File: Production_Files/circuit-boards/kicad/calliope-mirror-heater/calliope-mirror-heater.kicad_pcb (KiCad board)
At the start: 2 copper layers, 49 x 67 mm, 67 parts, among them J1 USB_C_Receptacle_USB2.0_16P, J2 Conn_02x15_Odd_Even, SW1 select-heater-power-source, U1 LM358DR2G, U2 TP5709S5, U3 XC6206P332MR-G, U4 GAQY212GSX

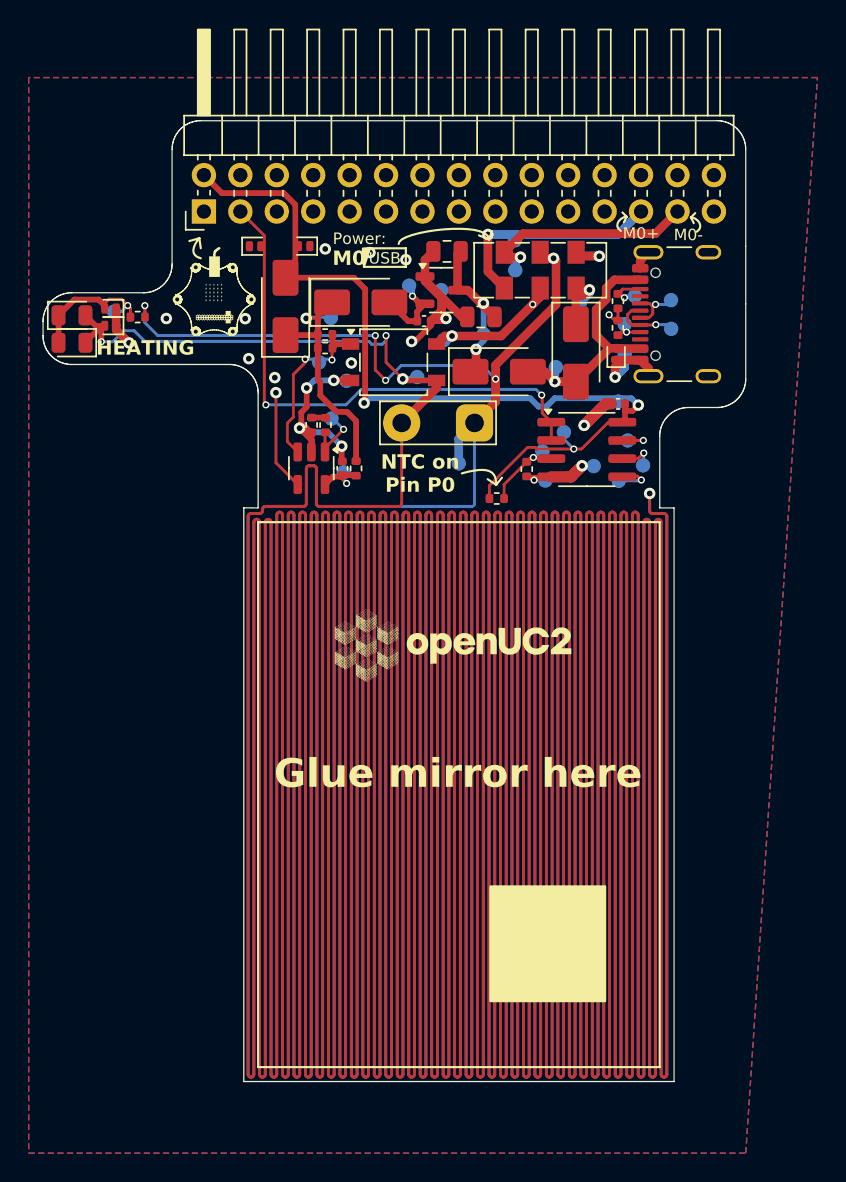
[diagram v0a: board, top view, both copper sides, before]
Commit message: Finished Rev B: correct slide-switch fp
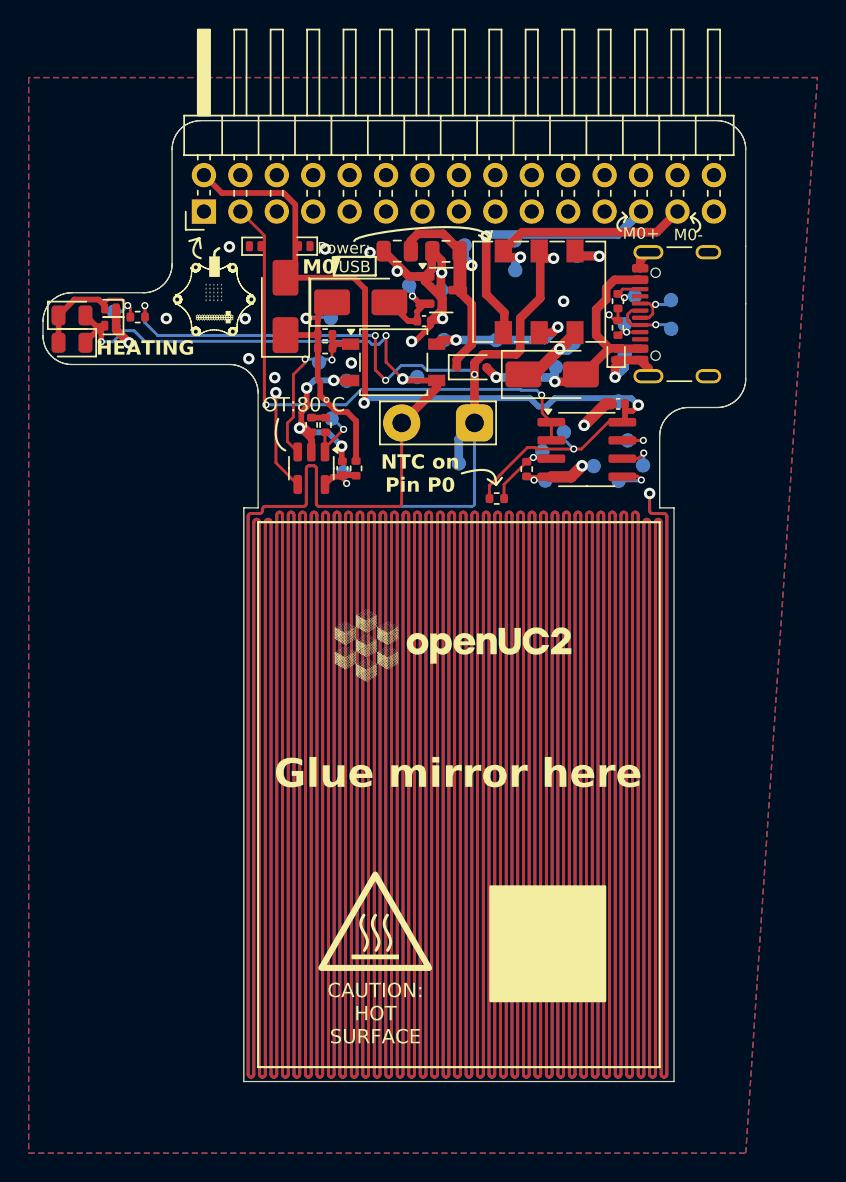
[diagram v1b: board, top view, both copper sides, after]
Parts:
- D4: value SS34 -> 1N5819WS; footprint Diode_SMD:D_SMA -> Diode_SMD:D_SOD-323
- moved C1 7.42 mm to (110.7, 82.1)
- moved TP10 6.35 mm to (115.4, 81.7)
- moved TP24 4.98 mm to (117.6, 88.3)
- moved TP25 2.83 mm to (123.0, 88.5)
- moved D7 2.24 mm to (121.5, 90.7), turned to 0 degrees
- moved D4 1.93 mm to (115.9, 90.2)
- moved SW1 1.50 mm to (120.6, 84.9)
- moved C3 0.07 mm to (114.1, 82.1)
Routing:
- net Net-(D4-K): track 11.4 -> 19.1 mm, vias 2 -> 1
- net GND: track 58.0 -> 62.4 mm, vias 22 -> 25
- net calliope_M0+: track 15.6 -> 18.8 mm
- net +5V_USB: track 17.6 -> 20.6 mm, vias 1 -> 2
- net Net-(D7-K): track 4.94 -> 6.00 mm
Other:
- board text added: "CAUTION: HOT SURFACE"
- board text added: "OT:80°C"
- board text added: "calliope-mirror-heater christiankuttke 2025-09-22; Rev. B openUC2 GmbH"
- board text removed: "calliope-mirror-heater christiankuttke 2025-09-22; Rev. A openUC2 GmbH"
